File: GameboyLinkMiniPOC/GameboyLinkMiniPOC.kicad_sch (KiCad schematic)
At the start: 6 parts, among them J2 AVR-ISP-6, SW1 SW_Reset, U1 ATtiny2313-20S

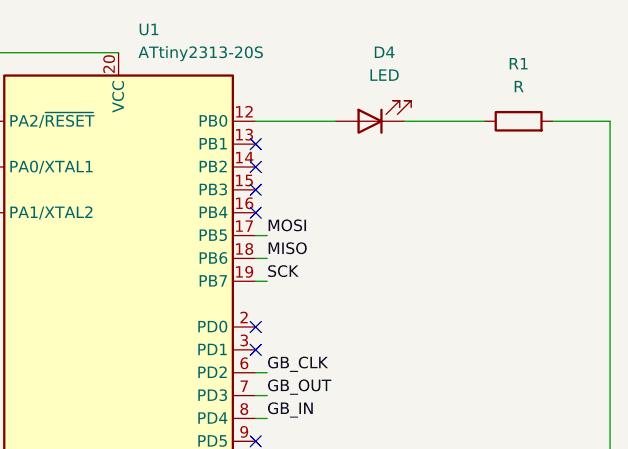
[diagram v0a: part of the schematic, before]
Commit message: Fixed passing (trench) of the GBA/Color Link connector, fixed the GB link mini PoC, resumed on the Link Mini.
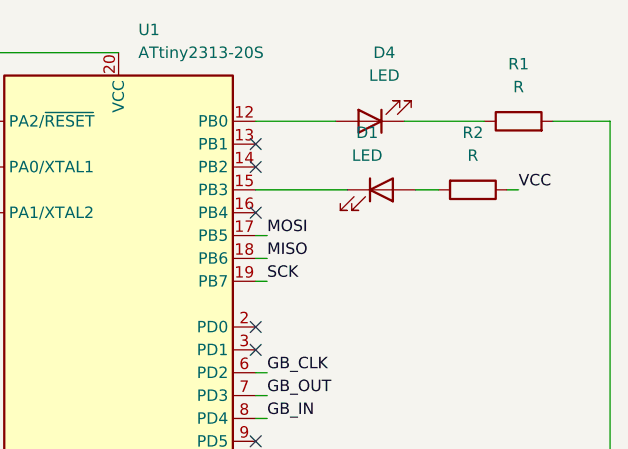
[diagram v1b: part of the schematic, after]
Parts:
- added D1: LED, LED_SMD:LED_1206_3216Metric_Pad1.42x1.75mm_HandSolder, symbol Device:LED
- added R2: R, Resistor_SMD:R_1206_3216Metric_Pad1.30x1.75mm_HandSolder, symbol Device:R
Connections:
- net VCC: now also R2.1
- net at U1.15 (PB3): now also D1.1 (K)
- new net: D1.2 (A), R2.2
- no-connect marks 11 -> 10
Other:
- company: (none) -> electrogeek.cc
- title: (none) -> Gameboy Link Mini - POC
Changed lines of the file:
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@@
 	(generator_version "8.0")
 	(paper "A4")
+	(title_block
+		(title "Gameboy Link Mini - POC")
+		(date "2024-05-25")
+		(company "electrogeek.cc")
+	)
 	(junction
 		(at 140.97 125.73)
@@
 	)
 	(no_connect
-		(at 156.21 85.09)
-	)
-	(no_connect
 		(at 156.21 87.63)
 	)
@@
 	(wire
 		(pts
+			(xy 173.99 85.09) (xy 176.53 85.09)
+		)
+		(stroke
+			(width 0)
+			(type default)
+		)
+	)
+	(wire
+		(pts
 			(xy 156.21 130.81) (xy 156.21 133.35)
 		)
@@
 	(wire
 		(pts
+			(xy 156.21 85.09) (xy 166.37 85.09)
+		)
+		(stroke
+			(width 0)
+			(type default)
+		)
+	)
+	(wire
+		(pts
 			(xy 157.48 105.41) (xy 156.21 105.41)
 		)
@@
 		(pts
 			(xy 124.46 125.73) (xy 140.97 125.73)
+		)
+		(stroke
+			(width 0)
+			(type default)
+		)
+	)
+	(wire
+		(pts
+			(xy 184.15 85.09) (xy 185.42 85.09)
 		)
 		(stroke
@@
 	(label "~RESET"
 		(at 171.45 148.59 0)
+		(fields_autoplaced yes)
+		(effects
+			(font
+				(size 1.27 1.27)
+			)
+			(justify left bottom)
+		)
+	)
+	(label "VCC"
+		(at 185.42 85.09 0)
 		(fields_autoplaced yes)
 		(effects
@@
 	)
 	(symbol
+		(lib_id "Device:LED")
+		(at 170.18 85.09 0)
+		(unit 1)
+		(exclude_from_sim no)
+		(in_bom yes)
+		(on_board yes)
+		(dnp no)
+		(fields_autoplaced yes)
+		(property "Reference" "D1"
+			(at 168.5925 78.74 0)
+			(effects
+				(font
+					(size 1.27 1.27)
+				)
+			)
+		)
+		(property "Value" "LED"
+			(at 168.5925 81.28 0)
+			(effects
+				(font
+					(size 1.27 1.27)
+				)
+			)
+		)
+		(property "Footprint" "LED_SMD:LED_1206_3216Metric_Pad1.42x1.75mm_HandSolder"
+			(at 170.18 85.09 0)
+			(effects
+				(font
+					(size 1.27 1.27)
+				)
+				(hide yes)
+			)
+		)
+		(property "Datasheet" "~"
+			(at 170.18 85.09 0)
+			(effects
+				(font
+					(size 1.27 1.27)
+				)
+				(hide yes)
+			)
+		)
+		(property "Description" "Light emitting diode"
+			(at 170.18 85.09 0)
+			(effects
+				(font
+					(size 1.27 1.27)
+				)
+				(hide yes)
+			)
+		)
+		(pin "2"
+		)
+		(pin "1"
+		)
+		(instances
+			(project "GameboyLinkMiniPOC"
+				(path "/1bf225e1-1dd2-400c-a06b-aef11d7813a0"
+					(reference "D1")
+					(unit 1)
+				)
+			)
+		)
+	)
+	(symbol
 		(lib_id "Switch:SW_Push")
 		(at 114.3 77.47 0)
@@
 					(unit 1)
 				)
+			)
+		)
+	)
+	(symbol
+		(lib_id "Device:R")
+		(at 180.34 85.09 270)
+		(unit 1)
+		(exclude_from_sim no)
+		(in_bom yes)
+		(on_board yes)
+		(dnp no)
+		(fields_autoplaced yes)
+		(property "Reference" "R2"
+			(at 180.34 78.74 90)
+			(effects
+				(font
+					(size 1.27 1.27)
+				)
+			)
+		)
+		(property "Value" "R"
+			(at 180.34 81.28 90)
+			(effects
+				(font
+					(size 1.27 1.27)
+				)
+			)
+		)
+		(property "Footprint" "Resistor_SMD:R_1206_3216Metric_Pad1.30x1.75mm_HandSolder"
+			(at 180.34 83.312 90)
+			(effects
+				(font
+					(size 1.27 1.27)
+				)
+				(hide yes)
+			)
+		)
+		(property "Datasheet" "~"
+			(at 180.34 85.09 0)
+			(effects
+				(font
+					(size 1.27 1.27)
+				)
+				(hide yes)
+			)
+		)
+		(property "Description" "Resistor"
+			(at 180.34 85.09 0)
+			(effects
+				(font
+					(size 1.27 1.27)
+				)
+				(hide yes)
+			)
+		)
+		(pin "2"
+		)
+		(pin "1"
+		)
+		(instances
+			(project "GameboyLinkMiniPOC"
+				(path "/1bf225e1-1dd2-400c-a06b-aef11d7813a0"
+					(reference "R2")
+					(unit 1)
+				)
